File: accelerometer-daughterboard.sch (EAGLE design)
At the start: 11 parts, among them U1 LIS3DHTR

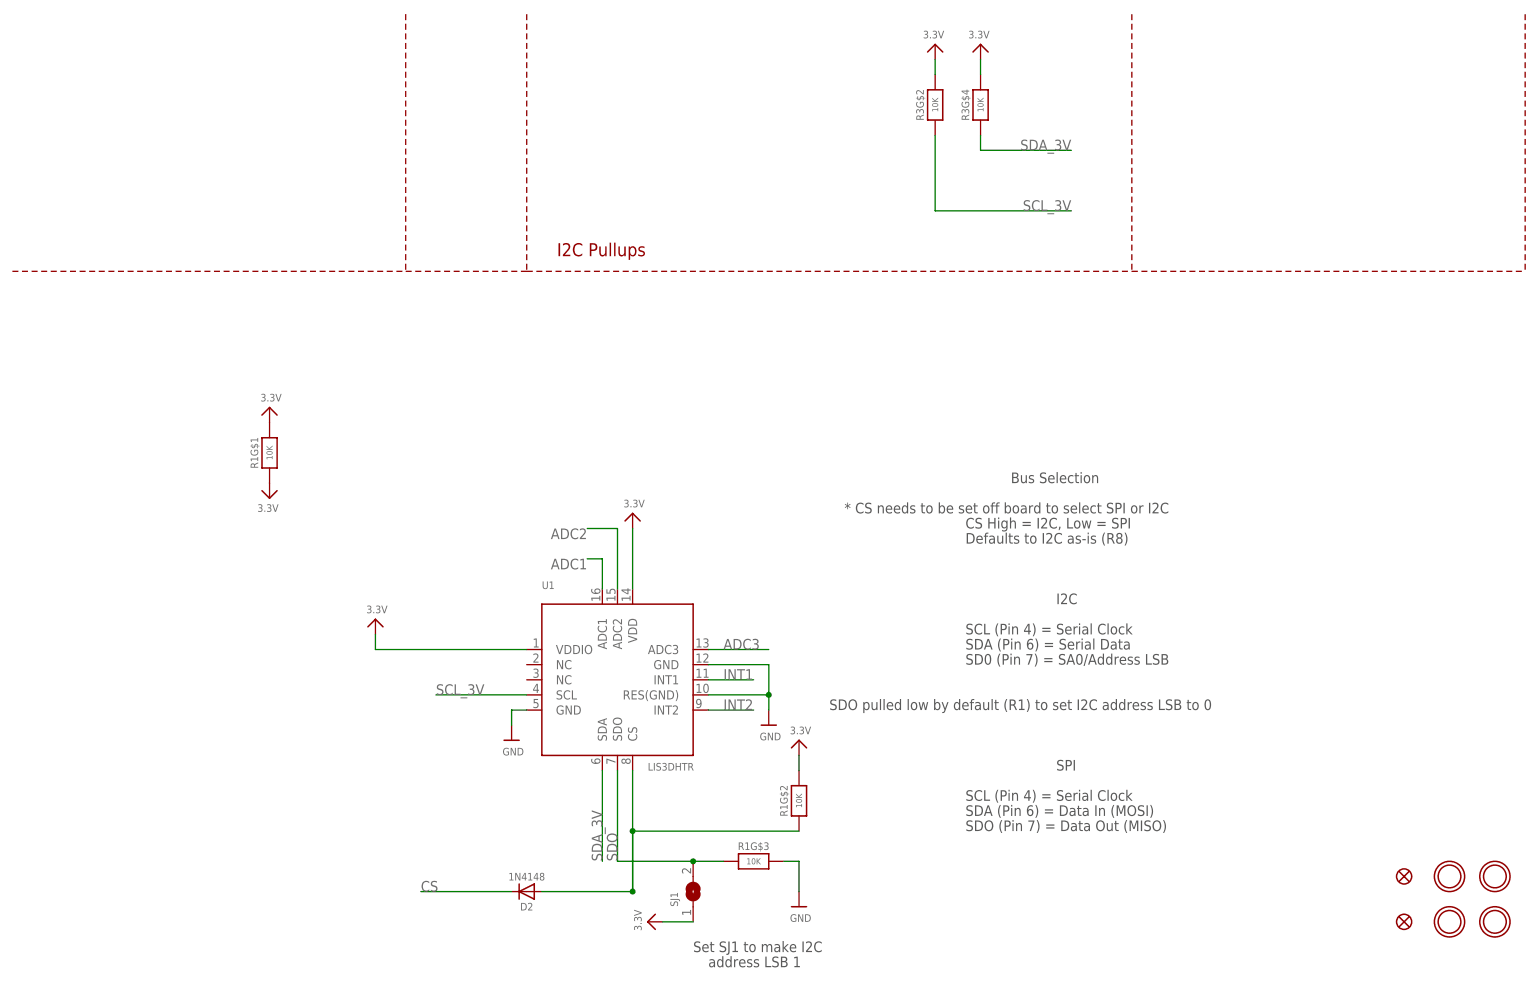
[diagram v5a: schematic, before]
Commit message: Hardwire CS to I2C mode; add pads; remove un-used board elements
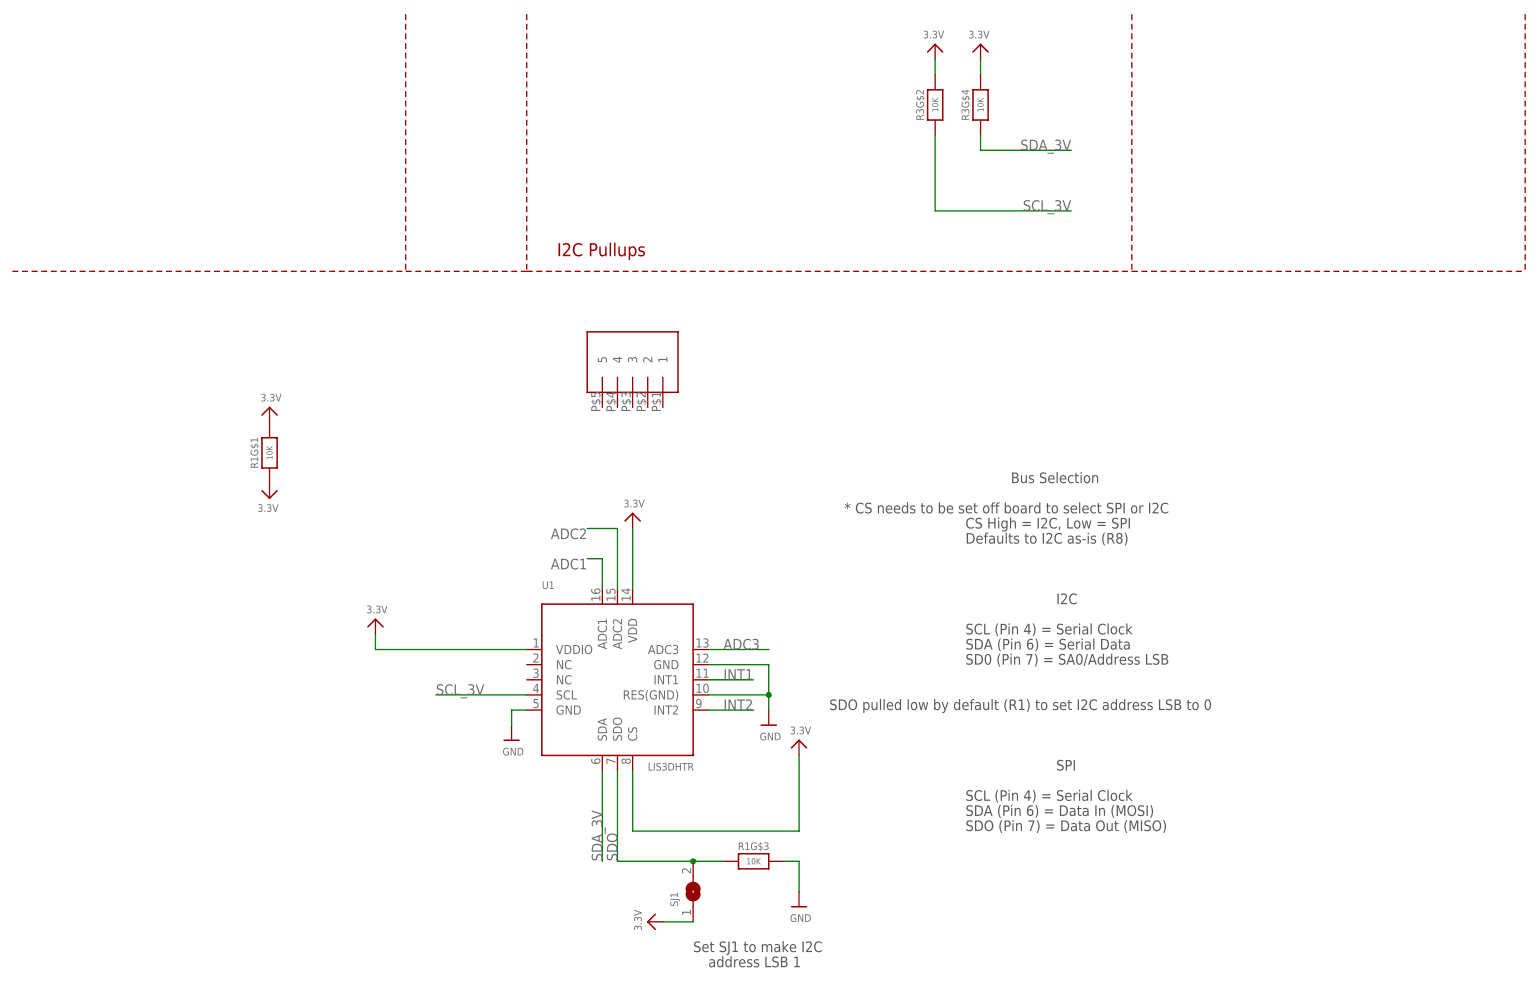
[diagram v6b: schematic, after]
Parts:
- removed D2: 1N4148, microbuilder:DIODESOD-323
- removed FID3, FID4: FIDUCIAL_1MM, microbuilder:FIDUCIAL_1MM
- removed U$17, U$19, U$21: MOUNTINGHOLE2.5, microbuilder:MOUNTINGHOLE2.5
- U$1: value MOUNTINGHOLE2.5 -> ALEX_CONN5; device microbuilder:MOUNTINGHOLE2.5 -> TestBoard_2_2_LiPo:ALEX_CONN5
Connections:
- removed net CS: D2.C
- removed net N$2: D2.A, R1G$2.1, U1.CS
- net 3.3V: now also U1.CS; no longer R1G$2.2
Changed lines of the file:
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@@
 <layer number="59" name="tCarbon" color="7" fill="1" visible="no" active="no"/>
 <layer number="60" name="bCarbon" color="7" fill="1" visible="no" active="no"/>
+<layer number="61" name="stand" color="7" fill="1" visible="no" active="no"/>
 <layer number="88" name="SimResults" color="9" fill="1" visible="yes" active="yes"/>
 <layer number="89" name="SimProbes" color="9" fill="1" visible="yes" active="yes"/>
@@
 <layer number="154" name="FabDoc2" color="2" fill="1" visible="no" active="no"/>
 <layer number="155" name="FabDoc3" color="7" fill="15" visible="no" active="no"/>
+<layer number="156" name="gesam-Maß" color="7" fill="1" visible="yes" active="yes"/>
+<layer number="157" name="FaceMchng" color="7" fill="1" visible="yes" active="yes"/>
+<layer number="158" name="FaceMMeas" color="7" fill="1" visible="yes" active="yes"/>
+<layer number="159" name="Geh-Bear2" color="7" fill="1" visible="yes" active="yes"/>
+<layer number="160" name="Topologie" color="7" fill="1" visible="yes" active="yes"/>
+<layer number="161" name="tomplace2" color="7" fill="1" visible="yes" active="yes"/>
 <layer number="166" name="AntennaArea" color="7" fill="1" visible="yes" active="yes"/>
 <layer number="168" name="4mmHeightArea" color="7" fill="1" visible="yes" active="yes"/>
@@
 <layer number="250" name="Descript" color="7" fill="1" visible="no" active="yes"/>
 <layer number="251" name="SMDround" color="7" fill="1" visible="no" active="yes"/>
+<layer number="252" name="BR-BS" color="7" fill="1" visible="yes" active="yes"/>
+<layer number="253" name="BR-LS" color="7" fill="1" visible="yes" active="yes"/>
 <layer number="254" name="cooling" color="7" fill="1" visible="no" active="yes"/>
 <layer number="255" name="routoute" color="7" fill="1" visible="yes" active="yes"/>
 </layers>
-<schematic xreflabel="%N (%S.%C%R)" xrefpart="/%S.%C%R">
+<schematic xreflabel="%F%N/%S.%C%R" xrefpart="/%S.%C%R">
 <attributes>
-<attribute name="COMPANY" value="ADAFRUIT INDUSTRIES"/>
+<attribute name="COMPANY" value=""/>
 <attribute name="DRAWN" value="KTOWN"/>
 <attribute name="REV" value="A"/>
@@
 <part name="U$24" library="microbuilder" deviceset="3.3V" device=""/>
 <part name="R3" library="microbuilder" deviceset="RESISTOR_4PACK" device="" value="10K"/>
-<part name="U$1" library="microbuilder" deviceset="MOUNTINGHOLE" device="2.5"/>
-<part name="U$17" library="microbuilder" deviceset="MOUNTINGHOLE" device="2.5"/>
 <part name="U$18" library="microbuilder" deviceset="FRAME_A4_ADAFRUIT" device=""/>
-<part name="FID3" library="microbuilder" deviceset="FIDUCIAL" device="_1MM"/>
-<part name="FID4" library="microbuilder" deviceset="FIDUCIAL" device="_1MM"/>
-<part name="U$19" library="microbuilder" deviceset="MOUNTINGHOLE" device="2.5"/>
-<part name="U$21" library="microbuilder" deviceset="MOUNTINGHOLE" device="2.5"/>
 <part name="U1" library="microbuilder" deviceset="ACCEL_LIS3DHTR" device="" value="LIS3DHTR"/>
 <part name="U$2" library="microbuilder" deviceset="GND" device=""/>
@@
 <part name="U$8" library="microbuilder" deviceset="3.3V" device=""/>
 <part name="U$11" library="microbuilder" deviceset="3.3V" device=""/>
-<part name="D2" library="microbuilder" deviceset="DIODE" device="SOD-323" value="1N4148"/>
 <part name="U$20" library="microbuilder" deviceset="3.3V" device=""/>
 <part name="U$27" library="microbuilder" deviceset="GND" device=""/>
@@
 <part name="SJ1" library="microbuilder" deviceset="SOLDERJUMPER" device=""/>
 <part name="U$22" library="microbuilder" deviceset="3.3V" device=""/>
+<part name="U$1" library="TestBoard_2_2_LiPo" deviceset="ALEX_CONN5" device=""/>
 </parts>
 <sheets>
@@
 </plain>
 <instances>
-<instance part="U$1" gate="G$1" x="243.84" y="22.86" smashed="yes"/>
-<instance part="U$17" gate="G$1" x="243.84" y="30.48" smashed="yes"/>
 <instance part="U$18" gate="G$1" x="0" y="0" smashed="yes">
 <attribute name="DRAWING_NAME" x="171.45" y="15.24" size="2.54" layer="94" font="vector"/>
@@
 <attribute name="SHEET" x="230.505" y="10.16" size="2.54" layer="94" font="vector"/>
 </instance>
-<instance part="FID3" gate="G$1" x="236.22" y="22.86" smashed="yes"/>
-<instance part="FID4" gate="G$1" x="236.22" y="30.48" smashed="yes"/>
-<instance part="U$19" gate="G$1" x="251.46" y="30.48" smashed="yes"/>
-<instance part="U$21" gate="G$1" x="251.46" y="22.86" smashed="yes"/>
 <instance part="U$7" gate="G$1" x="165.1" y="170.18" smashed="yes" rot="MR0">
 <attribute name="VALUE" x="166.624" y="171.196" size="1.27" layer="96" rot="MR0"/>
@@
 <attribute name="VALUE" x="61.976" y="74.676" size="1.27" layer="96"/>
 </instance>
-<instance part="D2" gate="G$1" x="88.9" y="27.94" smashed="yes" rot="R180">
-<attribute name="NAME" x="88.9" y="25.4" size="1.27" layer="95" rot="R180" align="center"/>
-<attribute name="VALUE" x="88.9" y="30.44" size="1.27" layer="96" rot="R180" align="center"/>
-</instance>
 <instance part="U$20" gate="G$1" x="134.62" y="53.34" smashed="yes">
 <attribute name="VALUE" x="133.096" y="54.356" size="1.27" layer="96"/>
@@
 <attribute name="VALUE" x="127" y="33.02" size="1.016" layer="96" font="vector" ratio="15" align="center"/>
 </instance>
-<instance part="R1" gate="G$2" x="134.62" y="43.18" smashed="yes" rot="R90">
-<attribute name="NAME" x="132.08" y="43.18" size="1.27" layer="95" font="vector" rot="R90" align="center"/>
-<attribute name="VALUE" x="134.62" y="43.18" size="1.016" layer="96" font="vector" ratio="15" rot="R90" align="center"/>
-</instance>
 <instance part="U$9" gate="G$1" x="45.72" y="109.22" smashed="yes">
 <attribute name="VALUE" x="44.196" y="110.236" size="1.27" layer="96"/>
@@
 <attribute name="VALUE" x="108.204" y="21.336" size="1.27" layer="96" rot="R90"/>
 </instance>
+<instance part="U$1" gate="G$1" x="104.14" y="114.3" smashed="yes" rot="R270"/>
 </instances>
 <busses>
@@
 <segment>
 <pinref part="U$20" gate="G$1" pin="3.3V"/>
-<wire x1="134.62" y1="48.26" x2="134.62" y2="50.8" width="0.1524" layer="91"/>
-<pinref part="R1" gate="G$2" pin="2"/>
+<pinref part="U1" gate="G$1" pin="CS"/>
+<wire x1="106.68" y1="38.1" x2="106.68" y2="48.26" width="0.1524" layer="91"/>
+<wire x1="134.62" y1="38.1" x2="106.68" y2="38.1" width="0.1524" layer="91"/>
+<wire x1="134.62" y1="38.1" x2="134.62" y2="50.8" width="0.1524" layer="91"/>
 </segment>
 <segment>
@@
 </segment>
 </net>
-<net name="CS" class="0">
-<segment>
-<pinref part="D2" gate="G$1" pin="C"/>
-<wire x1="86.36" y1="27.94" x2="71.12" y2="27.94" width="0.1524" layer="91"/>
-<label x="71.12" y="27.94" size="1.778" layer="95"/>
-</segment>
-</net>
-<net name="N$2" class="0">
-<segment>
-<pinref part="D2" gate="G$1" pin="A"/>
-<pinref part="U1" gate="G$1" pin="CS"/>
-<wire x1="91.44" y1="27.94" x2="106.68" y2="27.94" width="0.1524" layer="91"/>
-<wire x1="106.68" y1="27.94" x2="106.68" y2="38.1" width="0.1524" layer="91"/>
-<wire x1="106.68" y1="38.1" x2="106.68" y2="48.26" width="0.1524" layer="91"/>
-<wire x1="134.62" y1="38.1" x2="106.68" y2="38.1" width="0.1524" layer="91"/>
-<wire x1="106.68" y1="38.1" x2="106.68" y2="27.94" width="0.1524" layer="91"/>
-<junction x="106.68" y="27.94"/>
-<pinref part="R1" gate="G$2" pin="1"/>
-<junction x="106.68" y="38.1"/>
-</segment>
-</net>

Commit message: USe 0603 resistors
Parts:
- removed R1, R3: 10K, microbuilder:RESISTOR_4PACK
- removed SJ1: (no value), microbuilder:SOLDERJUMPER
- added R32, R34: 10K, rcl:R-EU_R0603
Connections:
- net 3.3V: now also R32.2, R34.2; no longer R1G$1.1, R1G$1.2, R3G$2.1, R3G$4.1, SJ1.1
- net GND: no longer R1G$3.2
- net SCL_3V: now also R32.1; no longer R3G$2.2
- net SDA_3V: now also R34.1; no longer R3G$4.2
- net SDO: no longer R1G$3.1, SJ1.2
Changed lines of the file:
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@@
 <part name="U$7" library="microbuilder" deviceset="3.3V" device=""/>
 <part name="U$24" library="microbuilder" deviceset="3.3V" device=""/>
-<part name="R3" library="microbuilder" deviceset="RESISTOR_4PACK" device="" value="10K"/>
 <part name="U$18" library="microbuilder" deviceset="FRAME_A4_ADAFRUIT" device=""/>
 <part name="U1" library="microbuilder" deviceset="ACCEL_LIS3DHTR" device="" value="LIS3DHTR"/>
@@
 <part name="U$11" library="microbuilder" deviceset="3.3V" device=""/>
 <part name="U$20" library="microbuilder" deviceset="3.3V" device=""/>
-<part name="U$27" library="microbuilder" deviceset="GND" device=""/>
-<part name="R1" library="microbuilder" deviceset="RESISTOR_4PACK" device="" value="10K"/>
-<part name="U$9" library="microbuilder" deviceset="3.3V" device=""/>
-<part name="U$10" library="microbuilder" deviceset="3.3V" device=""/>
-<part name="SJ1" library="microbuilder" deviceset="SOLDERJUMPER" device=""/>
-<part name="U$22" library="microbuilder" deviceset="3.3V" device=""/>
 <part name="U$1" library="TestBoard_2_2_LiPo" deviceset="ALEX_CONN5" device=""/>
+<part name="R32" library="rcl" library_urn="urn:adsk.eagle:library:334" deviceset="R-EU_" device="R0603" package3d_urn="urn:adsk.eagle:package:23555/3" value="10K"/>
+<part name="R34" library="rcl" library_urn="urn:adsk.eagle:library:334" deviceset="R-EU_" device="R0603" package3d_urn="urn:adsk.eagle:package:23555/3" value="10K"/>
 </parts>
 <sheets>
@@
 <attribute name="VALUE" x="159.004" y="171.196" size="1.27" layer="96" rot="MR0"/>
 </instance>
-<instance part="R3" gate="G$4" x="165.1" y="160.02" smashed="yes" rot="MR270">
-<attribute name="NAME" x="162.56" y="160.02" size="1.27" layer="95" font="vector" rot="MR270" align="center"/>
-<attribute name="VALUE" x="165.1" y="160.02" size="1.016" layer="96" font="vector" ratio="15" rot="MR270" align="center"/>
-</instance>
-<instance part="R3" gate="G$2" x="157.48" y="160.02" smashed="yes" rot="MR270">
-<attribute name="NAME" x="154.94" y="160.02" size="1.27" layer="95" font="vector" rot="MR270" align="center"/>
-<attribute name="VALUE" x="157.48" y="160.02" size="1.016" layer="96" font="vector" ratio="15" rot="MR270" align="center"/>
-</instance>
 <instance part="U1" gate="G$1" x="104.14" y="63.5" smashed="yes">
 <attribute name="NAME" x="91.44" y="78.74" size="1.27" layer="95"/>
@@
 <attribute name="VALUE" x="133.096" y="54.356" size="1.27" layer="96"/>
 </instance>
-<instance part="U$27" gate="G$1" x="134.62" y="25.4" smashed="yes">
-<attribute name="VALUE" x="133.096" y="22.86" size="1.27" layer="96"/>
-</instance>
-<instance part="R1" gate="G$1" x="45.72" y="101.6" smashed="yes" rot="R90">
-<attribute name="NAME" x="43.18" y="101.6" size="1.27" layer="95" font="vector" rot="R90" align="center"/>
-<attribute name="VALUE" x="45.72" y="101.6" size="1.016" layer="96" font="vector" ratio="15" rot="R90" align="center"/>
-</instance>
-<instance part="R1" gate="G$3" x="127" y="33.02" smashed="yes">
-<attribute name="NAME" x="127" y="35.56" size="1.27" layer="95" font="vector" align="center"/>
-<attribute name="VALUE" x="127" y="33.02" size="1.016" layer="96" font="vector" ratio="15" align="center"/>
-</instance>
-<instance part="U$9" gate="G$1" x="45.72" y="109.22" smashed="yes">
-<attribute name="VALUE" x="44.196" y="110.236" size="1.27" layer="96"/>
-</instance>
-<instance part="U$10" gate="G$1" x="45.72" y="93.98" smashed="yes" rot="R180">
-<attribute name="VALUE" x="47.244" y="92.964" size="1.27" layer="96" rot="R180"/>
-</instance>
-<instance part="SJ1" gate="1" x="116.84" y="27.94" smashed="yes" rot="R90">
-<attribute name="NAME" x="114.3" y="25.4" size="1.27" layer="95" rot="R90"/>
-<attribute name="VALUE" x="120.65" y="25.4" size="1.27" layer="96" rot="R90"/>
-</instance>
-<instance part="U$22" gate="G$1" x="109.22" y="22.86" smashed="yes" rot="R90">
-<attribute name="VALUE" x="108.204" y="21.336" size="1.27" layer="96" rot="R90"/>
-</instance>
 <instance part="U$1" gate="G$1" x="104.14" y="114.3" smashed="yes" rot="R270"/>
+<instance part="R32" gate="G$1" x="157.48" y="160.02" smashed="yes" rot="R90">
+<attribute name="NAME" x="155.9814" y="156.21" size="1.778" layer="95" rot="R90"/>
+<attribute name="VALUE" x="160.782" y="156.21" size="1.778" layer="96" rot="R90"/>
+</instance>
+<instance part="R34" gate="G$1" x="165.1" y="160.02" smashed="yes" rot="R90">
+<attribute name="NAME" x="163.6014" y="156.21" size="1.778" layer="95" rot="R90"/>
+<attribute name="VALUE" x="168.402" y="156.21" size="1.778" layer="96" rot="R90"/>
+</instance>
 </instances>
 <busses>
@@
 <junction x="129.54" y="60.96"/>
 </segment>
-<segment>
-<pinref part="U$27" gate="G$1" pin="GND"/>
-<wire x1="132.08" y1="33.02" x2="134.62" y2="33.02" width="0.1524" layer="91"/>
-<wire x1="134.62" y1="33.02" x2="134.62" y2="27.94" width="0.1524" layer="91"/>
-<pinref part="R1" gate="G$3" pin="2"/>
-</segment>
 </net>
 <net name="SCL_3V" class="0">
@@
 <wire x1="157.48" y1="142.24" x2="180.34" y2="142.24" width="0.1524" layer="91"/>
 <wire x1="157.48" y1="154.94" x2="157.48" y2="142.24" width="0.1524" layer="91"/>
-<pinref part="R3" gate="G$2" pin="2"/>
+<pinref part="R32" gate="G$1" pin="1"/>
 </segment>
 <segment>
@@
 <wire x1="165.1" y1="152.4" x2="180.34" y2="152.4" width="0.1524" layer="91"/>
 <wire x1="165.1" y1="154.94" x2="165.1" y2="152.4" width="0.1524" layer="91"/>
-<pinref part="R3" gate="G$4" pin="2"/>
+<pinref part="R34" gate="G$1" pin="1"/>
 </segment>
 <segment>
@@
 <pinref part="U$7" gate="G$1" pin="3.3V"/>
 <wire x1="165.1" y1="165.1" x2="165.1" y2="167.64" width="0.1524" layer="91"/>
-<pinref part="R3" gate="G$4" pin="1"/>
+<pinref part="R34" gate="G$1" pin="2"/>
 </segment>
 <segment>
 <pinref part="U$24" gate="G$1" pin="3.3V"/>
 <wire x1="157.48" y1="165.1" x2="157.48" y2="167.64" width="0.1524" layer="91"/>
-<pinref part="R3" gate="G$2" pin="1"/>
+<pinref part="R32" gate="G$1" pin="2"/>
 </segment>
 <segment>
@@
 <wire x1="134.62" y1="38.1" x2="134.62" y2="50.8" width="0.1524" layer="91"/>
 </segment>
-<segment>
-<pinref part="R1" gate="G$1" pin="2"/>
-<pinref part="U$9" gate="G$1" pin="3.3V"/>
-</segment>
-<segment>
-<pinref part="R1" gate="G$1" pin="1"/>
-<pinref part="U$10" gate="G$1" pin="3.3V"/>
-</segment>
-<segment>
-<pinref part="SJ1" gate="1" pin="1"/>
-<pinref part="U$22" gate="G$1" pin="3.3V"/>
-<wire x1="111.76" y1="22.86" x2="116.84" y2="22.86" width="0.1524" layer="91"/>
-</segment>
 </net>
 <net name="INT1" class="0">
@@
 <wire x1="104.14" y1="48.26" x2="104.14" y2="33.02" width="0.1524" layer="91"/>
 <label x="104.14" y="33.02" size="1.778" layer="95" rot="R90"/>
-<wire x1="104.14" y1="33.02" x2="116.84" y2="33.02" width="0.1524" layer="91"/>
-<pinref part="R1" gate="G$3" pin="1"/>
-<pinref part="SJ1" gate="1" pin="2"/>
-<wire x1="116.84" y1="33.02" x2="121.92" y2="33.02" width="0.1524" layer="91"/>
-<junction x="116.84" y="33.02"/>
 </segment>
 </net>
@@
 </schematic>
 </drawing>
+<compatibility>
+<note version="8.2" severity="warning">
+Since Version 8.2, EAGLE supports online libraries. The ids
+of those online libraries will not be understood (or retained)
+with this version.
+</note>
+<note version="8.3" severity="warning">
+Since Version 8.3, EAGLE supports URNs for individual library
+assets (packages, symbols, and devices). The URNs of those assets
+will not be understood (or retained) with this version.
+</note>
+<note version="8.3" severity="warning">
+Since Version 8.3, EAGLE supports the association of 3D packages
+with devices in libraries, schematics, and board files. Those 3D
+packages will not be understood (or retained) with this version.
+</note>
+<note version="8.4" severity="warning">
+Since Version 8.4, EAGLE supports properties for SPICE simulation.
+Probes in schematics and SPICE mapping objects found in parts and library devices
+will not be understood with this version. Update EAGLE to the latest version
+for full support of SPICE simulation.
+</note>
+</compatibility>
 </eagle>
